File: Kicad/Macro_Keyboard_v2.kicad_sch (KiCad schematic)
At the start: 85 parts, among them J1 Conn_01x04_Female, SW1 RESET SWITCH, SW10 SW_Push, SW11 SW_Push, SW12 SW_Push, SW13 SW_Push, SW14 SW_Push, SW15 SW_Push, SW16 SW_Push, SW17 SW_Push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

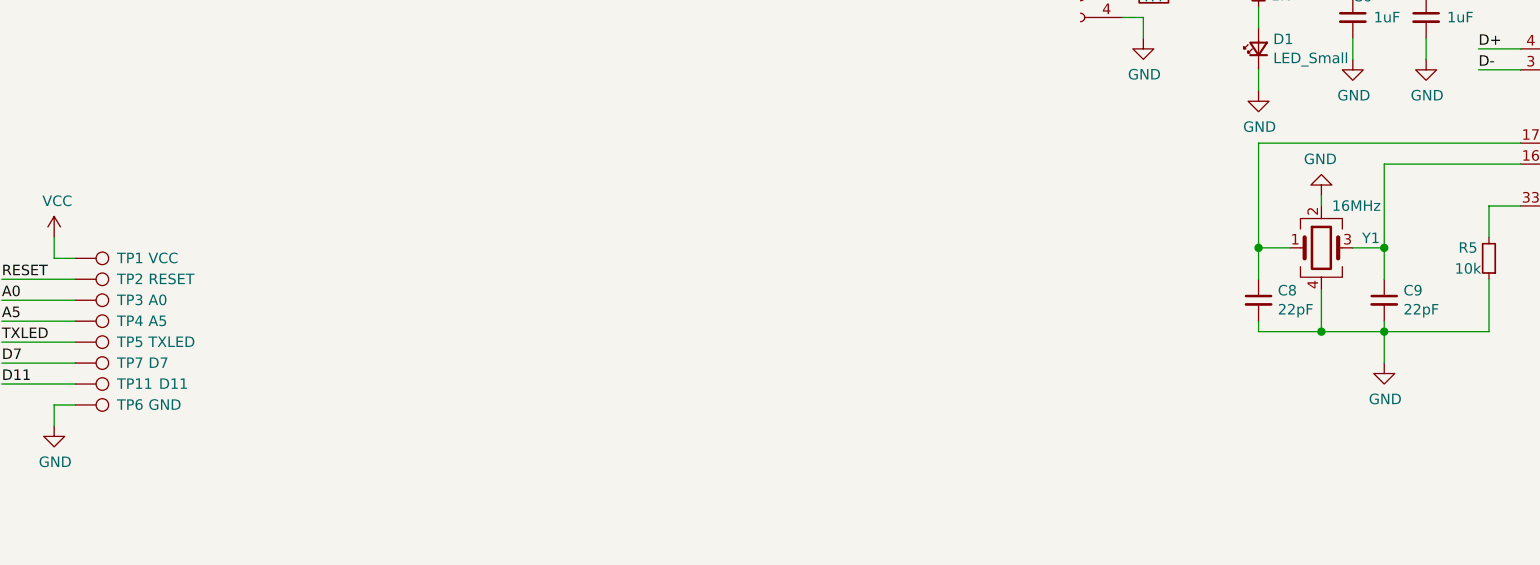
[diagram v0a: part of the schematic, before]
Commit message: little silkscreen update
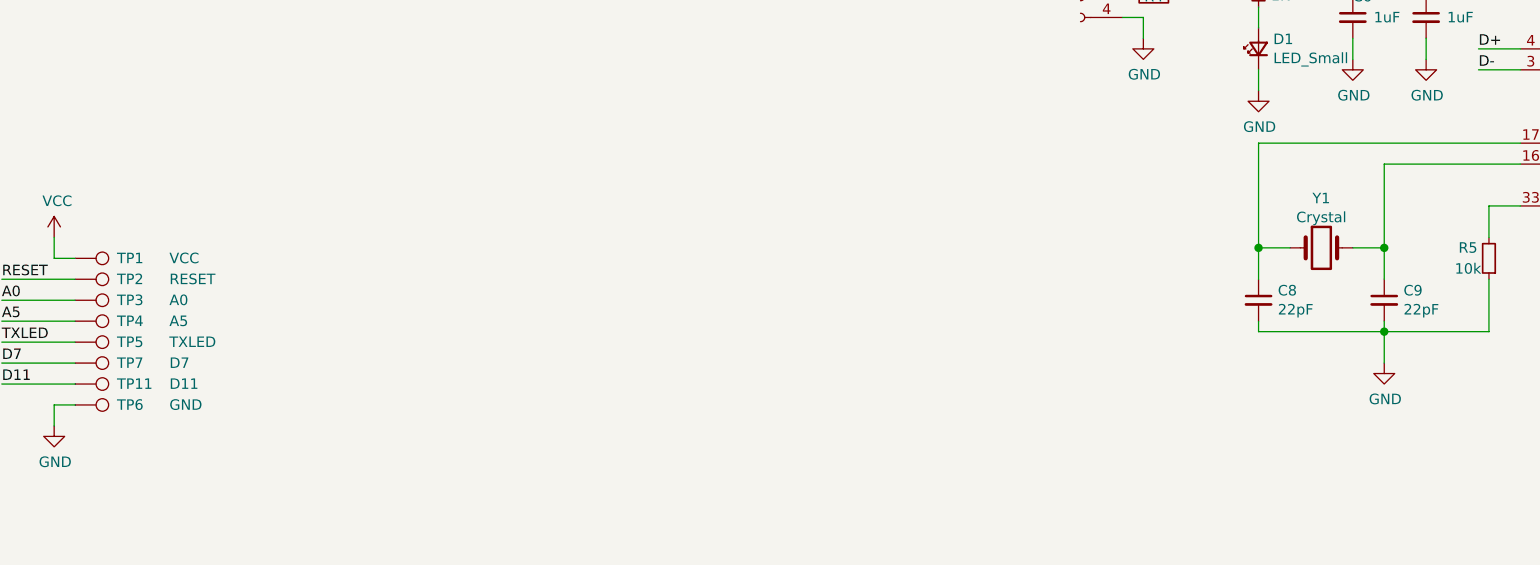
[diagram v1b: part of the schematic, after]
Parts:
- removed Y1: 16MHz, Crystal:Crystal_SMD_3225-4Pin_3.2x2.5mm, symbol Device:Crystal_GND24
- added Y1: Crystal, Crystal:Crystal_SMD_3225-4Pin_3.2x2.5mm, symbol Device:Crystal
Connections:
- net at C9.1, U1.16 (XTAL2): now also Y1.2
- net at C8.1, U1.17 (XTAL1): now also Y1.1
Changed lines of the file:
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@@
   (junction (at 181.61 78.74) (diameter 1.016) (color 0 0 0 0))
   (junction (at 181.61 114.3) (diameter 1.016) (color 0 0 0 0))
-  (junction (at 189.23 124.46) (diameter 1.016) (color 0 0 0 0))
   (junction (at 193.04 41.91) (diameter 1.016) (color 0 0 0 0))
   (junction (at 193.04 55.88) (diameter 1.016) (color 0 0 0 0))
@@
     (stroke (width 0) (type solid) (color 0 0 0 0))
   )
+  (wire (pts (xy 181.61 124.46) (xy 196.85 124.46))
+    (stroke (width 0) (type solid) (color 0 0 0 0))
+  )
   (wire (pts (xy 185.42 114.3) (xy 181.61 114.3))
     (stroke (width 0) (type solid) (color 0 0 0 0))
   )
-  (wire (pts (xy 189.23 109.22) (xy 189.23 107.95))
-    (stroke (width 0) (type solid) (color 0 0 0 0))
-  )
-  (wire (pts (xy 189.23 119.38) (xy 189.23 124.46))
-    (stroke (width 0) (type solid) (color 0 0 0 0))
-  )
-  (wire (pts (xy 189.23 124.46) (xy 181.61 124.46))
-    (stroke (width 0) (type solid) (color 0 0 0 0))
-  )
   (wire (pts (xy 193.04 41.91) (xy 193.04 35.56))
     (stroke (width 0) (type solid) (color 0 0 0 0))
@@
   )
   (wire (pts (xy 196.85 123.19) (xy 196.85 124.46))
-    (stroke (width 0) (type solid) (color 0 0 0 0))
-  )
-  (wire (pts (xy 196.85 124.46) (xy 189.23 124.46))
     (stroke (width 0) (type solid) (color 0 0 0 0))
   )
@@
       (effects (font (size 1.27 1.27)) (justify left))
     )
-    (property "Value" "VCC" (id 1) (at 46.99 115.57 90)
+    (property "Value" "VCC" (id 1) (at 49.53 115.57 90)
       (effects (font (size 1.27 1.27)) (justify left))
     )
@@
       (effects (font (size 1.27 1.27)) (justify left))
     )
-    (property "Value" "RESET" (id 1) (at 46.99 118.11 90)
+    (property "Value" "RESET" (id 1) (at 49.53 118.11 90)
       (effects (font (size 1.27 1.27)) (justify left))
     )
@@
       (effects (font (size 1.27 1.27)) (justify left))
     )
-    (property "Value" "A0" (id 1) (at 46.99 120.65 90)
+    (property "Value" "A0" (id 1) (at 49.53 120.65 90)
       (effects (font (size 1.27 1.27)) (justify left))
     )
@@
       (effects (font (size 1.27 1.27)) (justify left))
     )
-    (property "Value" "A5" (id 1) (at 46.99 123.19 90)
+    (property "Value" "A5" (id 1) (at 49.53 123.19 90)
       (effects (font (size 1.27 1.27)) (justify left))
     )
@@
       (effects (font (size 1.27 1.27)) (justify left))
     )
-    (property "Value" "TXLED" (id 1) (at 46.99 125.73 90)
+    (property "Value" "TXLED" (id 1) (at 49.53 125.73 90)
       (effects (font (size 1.27 1.27)) (justify left))
     )
@@
       (effects (font (size 1.27 1.27)) (justify left))
     )
-    (property "Value" "D7" (id 1) (at 46.99 128.27 90)
+    (property "Value" "D7" (id 1) (at 49.53 128.27 90)
       (effects (font (size 1.27 1.27)) (justify left))
     )
@@
       (effects (font (size 1.27 1.27)) (justify left))
     )
-    (property "Value" "D11" (id 1) (at 48.26 130.81 90)
+    (property "Value" "D11" (id 1) (at 49.53 130.81 90)
       (effects (font (size 1.27 1.27)) (justify left))
     )
@@
       (effects (font (size 1.27 1.27)) (justify left))
     )
-    (property "Value" "GND" (id 1) (at 46.99 133.35 90)
+    (property "Value" "GND" (id 1) (at 49.53 133.35 90)
       (effects (font (size 1.27 1.27)) (justify left))
     )
@@
     )
     (property "Datasheet" "" (id 3) (at 181.61 95.25 0)
-      (effects (font (size 1.27 1.27)) hide)
-    )
-    (pin "1")
-  )
-  (symbol (lib_id "power:GND") (at 189.23 107.95 180) (unit 1)
-    (in_bom yes) (on_board yes)
-    (property "Reference" "#PWR0121" (id 0) (at 189.23 101.6 0)
-      (effects (font (size 1.27 1.27)) hide)
-    )
-    (property "Value" "GND" (id 1) (at 189.103 103.5558 0))
-    (property "Footprint" "" (id 2) (at 189.23 107.95 0)
-      (effects (font (size 1.27 1.27)) hide)
-    )
-    (property "Datasheet" "" (id 3) (at 189.23 107.95 0)
       (effects (font (size 1.27 1.27)) hide)
     )
@@
     )
     (property "LCSC" "C92584" (id 4) (at 223.52 35.56 0)
+      (effects (font (size 1.27 1.27)) hide)
+    )
+    (pin "1")
+    (pin "2")
+  )
+  (symbol (lib_id "Device:Crystal") (at 189.23 114.3 0) (unit 1)
+    (in_bom yes) (on_board yes) (fields_autoplaced)
+    (property "Reference" "Y1" (id 0) (at 189.23 108.3014 0))
+    (property "Value" "Crystal" (id 1) (at 189.23 110.6001 0))
+    (property "Footprint" "Crystal:Crystal_SMD_3225-4Pin_3.2x2.5mm" (id 2) (at 189.23 114.3 0)
+      (effects (font (size 1.27 1.27)) hide)
+    )
+    (property "Datasheet" "~" (id 3) (at 189.23 114.3 0)
       (effects (font (size 1.27 1.27)) hide)
     )
@@
     )
     (property "Datasheet" "~" (id 3) (at 160.02 81.28 0)
-      (effects (font (size 1.27 1.27)) hide)
-    )
-    (pin "1")
-    (pin "2")
-    (pin "3")
-    (pin "4")
-  )
-  (symbol (lib_id "Device:Crystal_GND24") (at 189.23 114.3 0) (unit 1)
-    (in_bom yes) (on_board yes)
-    (property "Reference" "Y1" (id 0) (at 194.1576 113.1316 0)
-      (effects (font (size 1.27 1.27)) (justify left))
-    )
-    (property "Value" "16MHz" (id 1) (at 190.5 109.22 0)
-      (effects (font (size 1.27 1.27)) (justify left))
-    )
-    (property "Footprint" "Crystal:Crystal_SMD_3225-4Pin_3.2x2.5mm" (id 2) (at 189.23 114.3 0)
-      (effects (font (size 1.27 1.27)) hide)
-    )
-    (property "Datasheet" "https://datasheet.lcsc.com/szlcsc/Yangxing-Tech-X322516MOB4SI_C12668.pdf" (id 3) (at 189.23 114.3 0)
-      (effects (font (size 1.27 1.27)) hide)
-    )
-    (property "LCSC" "C15171" (id 4) (at 189.23 114.3 0)
       (effects (font (size 1.27 1.27)) hide)
     )
@@
       (reference "#PWR0120") (unit 1) (value "GND") (footprint "")
     )
-    (path "/00000000-0000-0000-0000-0000607dd3d4"
-      (reference "#PWR0121") (unit 1) (value "GND") (footprint "")
-    )
     (path "/00000000-0000-0000-0000-00006071e91e"
       (reference "C1") (unit 1) (value "1uF") (footprint "Capacitor_SMD:C_0603_1608Metric_Pad1.08x0.95mm_HandSolder")
@@
       (reference "U1") (unit 1) (value "atmega32u4-au") (footprint "Package_QFP:TQFP-44_10x10mm_P0.8mm")
     )
-    (path "/00000000-0000-0000-0000-000060742db7"
-      (reference "Y1") (unit 1) (value "16MHz") (footprint "Crystal:Crystal_SMD_3225-4Pin_3.2x2.5mm")
-    )
-  )
+    (path "/75937cba-7b47-402e-904c-8b129a818907"
+      (reference "Y1") (unit 1) (value "Crystal") (footprint "Crystal:Crystal_SMD_3225-4Pin_3.2x2.5mm")
+    )
+  )
